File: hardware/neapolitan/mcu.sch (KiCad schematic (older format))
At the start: 60 parts, among them J1 USB-MICRO-B, J11 BARREL_JACK, P1 !IO_INT, P2 !IO_RESET, P20 GPIO, P22 I2S, P28 SD, P5 LEDS, P80 SHIELD, Q5 MOSFET_P, U15 TCA6424A, X2 FOX924B, X3 KT2520, X4 OH4

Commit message: Neapolitan: schematic annotation and cleanup
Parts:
- gave numbers to parts that had none: 16
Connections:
- net ADC0_0: no longer names the net of P20.20 (P20)
- net ADC0_2: no longer names the net of P20.16 (P16)
- net ADC0_6: no longer names the net of P20.14 (P14)
- net CLKOUT: no longer names the net of P22.1 (P1)
- net GCK1: no longer names the net of P28.14 (P14)
- net GCK2: no longer names the net of P28.13 (P13)
- net GPIO3_10: no longer names the net of P20.7 (P7)
- net GPIO3_11: no longer names the net of P20.8 (P8)
- net GPIO3_12: no longer names the net of P20.9 (P9)
- net GPIO3_13: no longer names the net of P20.10 (P10)
- net GPIO3_14: no longer names the net of P20.11 (P11)
- net GPIO3_15: no longer names the net of P20.12 (P12)
- net GPIO3_8: no longer names the net of P20.5 (P5)
- net GPIO3_9: no longer names the net of P20.6 (P6)
- net I2S0_RX_MCLK: no longer names the net of P22.14 (P14)
- net I2S0_RX_SCK: no longer names the net of P22.12 (P12)
- net I2S0_RX_SDA: no longer names the net of P22.13 (P13)
- net I2S0_RX_WS: no longer names the net of P22.15 (P15)
- net I2S0_TX_MCLK: no longer names the net of P22.17 (P17)
- net I2S0_TX_SCK: no longer names the net of P22.16 (P16)
- net P2_13: no longer names the net of P22.22 (P22)
- net P2_8: no longer names the net of P22.23 (P23)
- net P2_9: no longer names the net of P22.21 (P21)
- net RESET: no longer names the net of P22.3 (P3)
- net RTC_ALARM: no longer names the net of P20.2 (P2)
- net SD_CD: no longer names the net of P28.3 (P3)
- net SD_CLK: no longer names the net of P28.11 (P11)
- net U0_RXD: no longer names the net of P22.19 (P19)
- net U0_TXD: no longer names the net of P22.20 (P20)
- net VBAT: no longer names the net of P20.1 (P1)
- net WAKEUP: no longer names the net of P20.4 (P4)
- no-connect marks 17 -> 48
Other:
- note removed: "/I2S0_TX_WS"
- note removed: "I2S0_TX_SDA/"
- moved on the sheet: C68, C69, C71, C72, C73, C74, C75, C76, L10, P1, P2, P20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

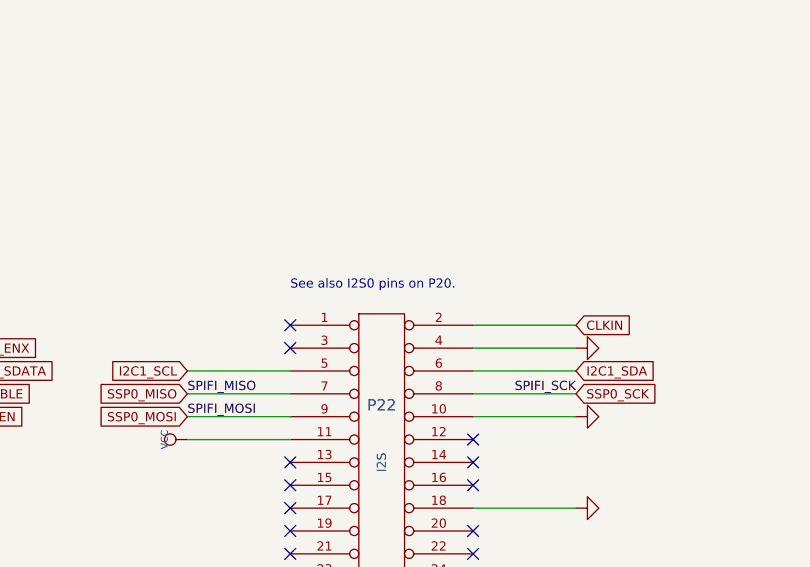
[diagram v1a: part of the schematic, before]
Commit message: Neapolitan: module assignment
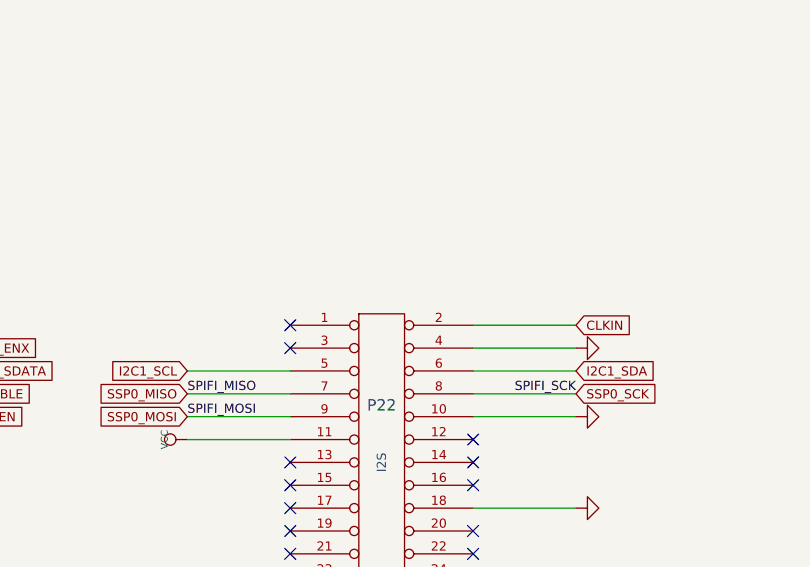
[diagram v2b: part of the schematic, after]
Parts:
- U16: footprint (none) -> gsg-modules:SOT25
- U18: footprint (none) -> gsg-modules:SOT353-1
- X2: footprint (none) -> gsg-modules:XTAL5.0x3.2mm; Description (none) -> OSC TCXO 10.000MHZ HCMOS SMD; Manufacturer (none) -> Fox Electronics; Part Number (none) -> FOX924B-10.000
- X3: footprint (none) -> gsg-modules:KT2520K
- X4: footprint (none) -> gsg-modules:OH4
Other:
- note removed: "See also I2S0 pins on P20."
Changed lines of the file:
@@
 	1    0    0    -1
 $EndComp
-Text Notes 9300 8100 0    40   ~ 0
-See also I2S0 pins on P20.
 Text GLabel 5500 3500 0    40   Input ~ 0
 MIX_BYPASS
@@
 F 0 "X2" H 9050 5050 60  0000 C CNN
 F 1 "FOX924B" H 9050 4750 60  0000 C CNN
-F 2 "" H 9050 4900 60  0000 C CNN
+F 2 "gsg-modules:XTAL5.0x3.2mm" H 9050 4900 60  0001 C CNN
 F 3 "" H 9050 4900 60  0000 C CNN
+F 4 "Fox Electronics" H 9050 4900 60  0001 C CNN "Manufacturer"
+F 5 "FOX924B-10.000" H 9050 4900 60  0001 C CNN "Part Number"
+F 6 "OSC TCXO 10.000MHZ HCMOS SMD" H 9050 4900 60  0001 C CNN "Description"
 	1    9050 4900
 	1    0    0    -1
@@
 F 0 "X3" H 11200 5800 60  0000 C CNN
 F 1 "KT2520" H 11200 5400 60  0000 C CNN
-F 2 "" H 11200 5600 60  0000 C CNN
+F 2 "gsg-modules:KT2520K" H 11200 5600 60  0001 C CNN
 F 3 "" H 11200 5600 60  0000 C CNN
 F 4 "AVX" H 11200 5600 60  0001 C CNN "Manufacturer"
@@
 F 0 "U16" H 11200 5100 40  0000 C CNN
 F 1 "TCR2EF" H 11200 4700 40  0000 C CNN
-F 2 "" H 11200 4900 40  0000 C CNN
+F 2 "gsg-modules:SOT25" H 11200 4900 40  0001 C CNN
 F 3 "" H 11200 4900 40  0000 C CNN
 F 4 "Toshiba" H 11200 4900 60  0001 C CNN "Manufacturer"
@@
 F 0 "U18" H 12895 5815 40  0000 C CNN
 F 1 "74LVC1G14" H 12950 5600 40  0000 C CNN
-F 2 "" H 12845 5565 30  0000 C CNN
+F 2 "gsg-modules:SOT353-1" H 12845 5565 30  0001 C CNN
 F 3 "" H 12895 5815 60  0000 C CNN
 F 4 "NXP" H 12750 5700 60  0001 C CNN "Manufacturer"
@@
 F 0 "X4" H 14700 4950 60  0000 C CNN
 F 1 "OH4" H 14700 4650 60  0000 C CNN
-F 2 "" H 14700 4800 60  0000 C CNN
+F 2 "gsg-modules:OH4" H 14700 4800 60  0001 C CNN
 F 3 "" H 14700 4800 60  0000 C CNN
 F 4 "Connor-Winfield" H 14700 4800 60  0001 C CNN "Manufacturer"

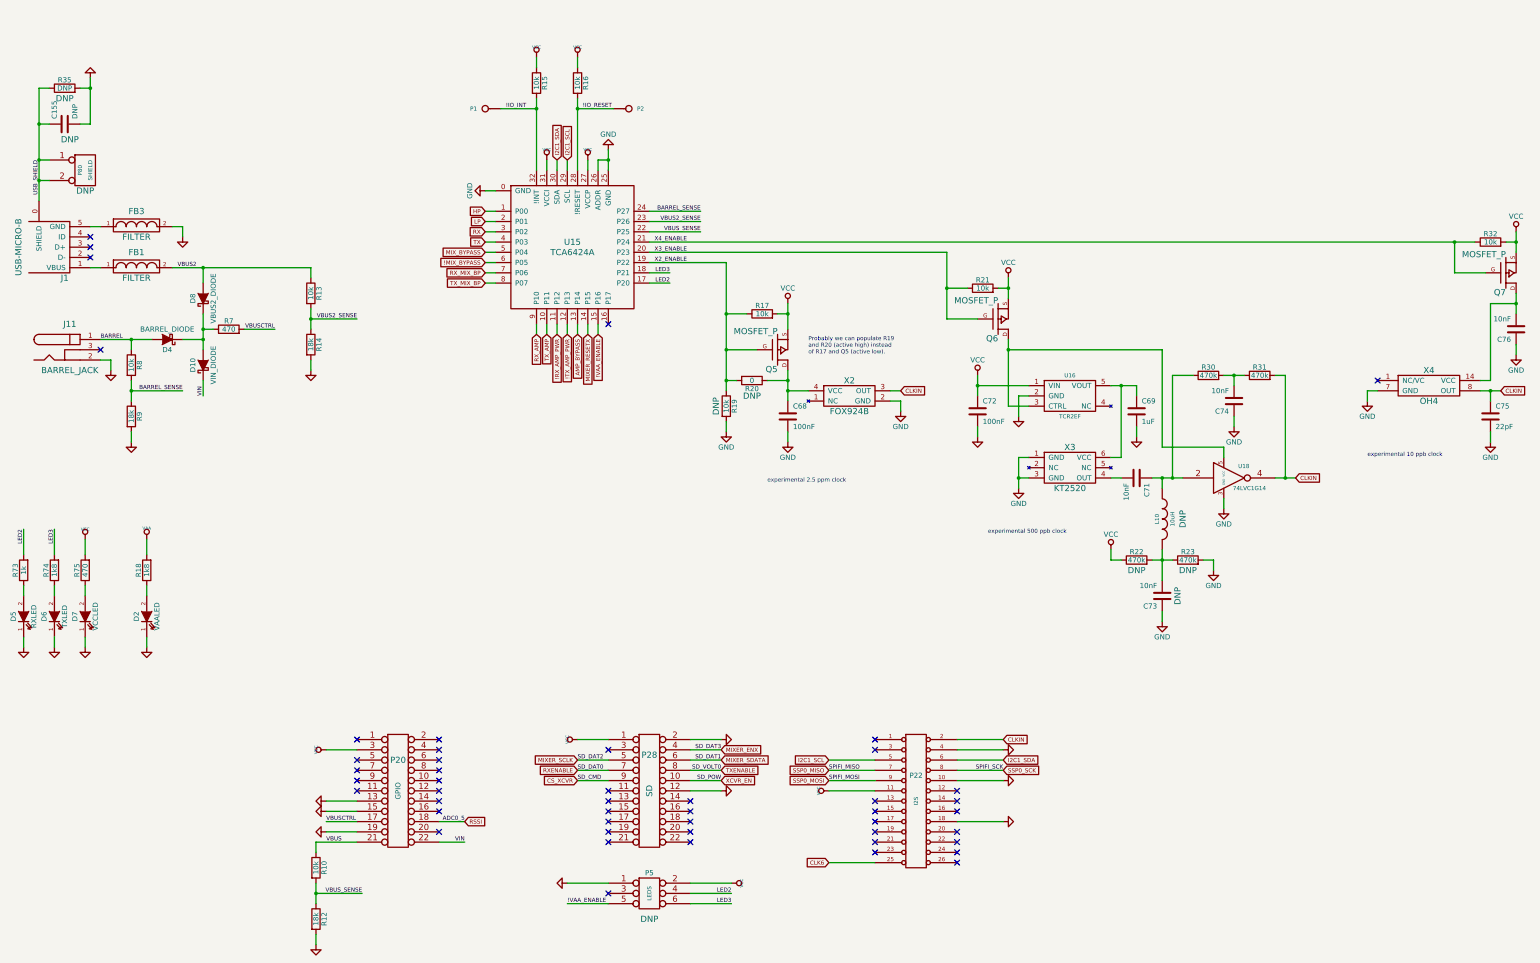
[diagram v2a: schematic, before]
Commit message: Neapolitan: completed initial layout
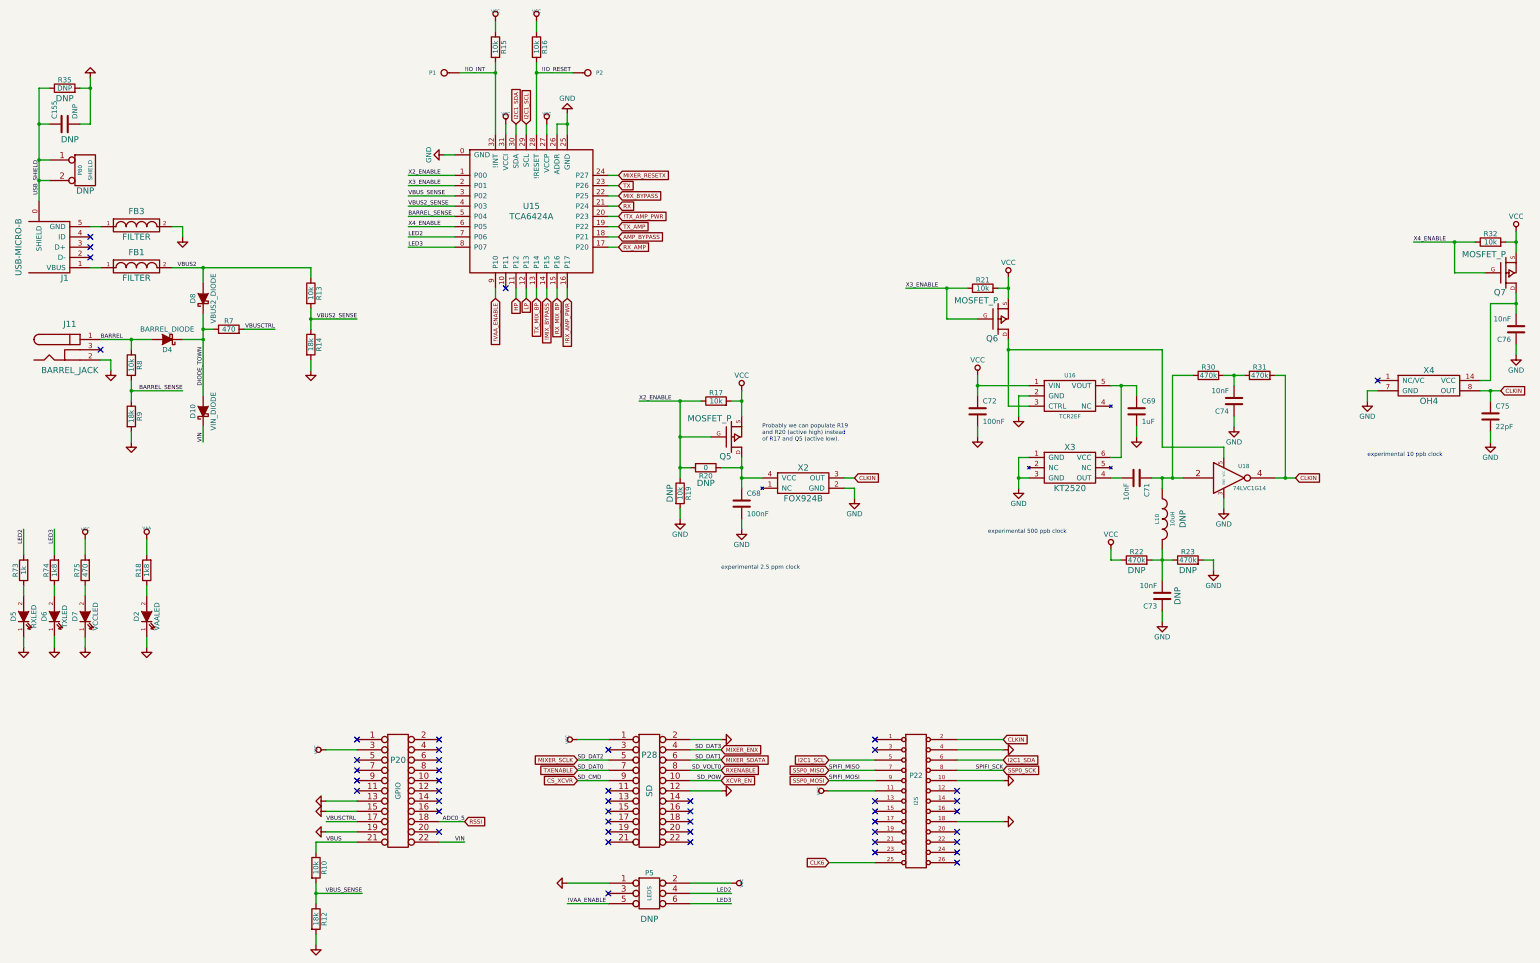
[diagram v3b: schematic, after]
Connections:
- net !MIX_BYPASS: now also U15.14 (P15); no longer U15.6 (P05)
- net !RX_AMP_PWR: now also U15.16 (P17); no longer U15.11 (P12)
- net !TX_AMP_PWR: now also U15.20 (P23); no longer U15.12 (P13)
- net !VAA_ENABLE: now also U15.9 (P10); no longer U15.15 (P16)
- net AMP_BYPASS: now also U15.18 (P21); no longer U15.13 (P14)
- net BARREL_SENSE: now also U15.5 (P04); no longer U15.24 (P27)
- net HP: now also U15.11 (P12); no longer U15.1 (P00)
- net LED2: now also U15.7 (P06); no longer U15.17 (P20)
- net LED3: now also U15.8 (P07); no longer U15.18 (P21)
- net LP: now also U15.12 (P13); no longer U15.2 (P01)
- net MIXER_RESETX: now also U15.24 (P27); no longer U15.14 (P15)
- net MIX_BYPASS: now also U15.22 (P25); no longer U15.5 (P04)
- net RX: now also U15.21 (P24); no longer U15.3 (P02)
- net RXENABLE: now also P28.8 (P8); no longer P28.7 (P7)
- net RX_AMP: now also U15.17 (P20); no longer U15.9 (P10)
- net RX_MIX_BP: now also U15.15 (P16); no longer U15.7 (P06)
- net TX: now also U15.23 (P26); no longer U15.4 (P03)
- net TXENABLE: now also P28.7 (P7); no longer P28.8 (P8)
- net TX_AMP: now also U15.19 (P22); no longer U15.10 (P11)
- net TX_MIX_BP: now also U15.13 (P14); no longer U15.8 (P07)
- net VBUS2_SENSE: now also U15.4 (P03); no longer U15.23 (P26)
- net VBUS_SENSE: now also U15.3 (P02); no longer U15.22 (P25)
- net X2_ENABLE: now also U15.1 (P00); no longer U15.19 (P22)
- net X3_ENABLE: now also U15.2 (P01); no longer U15.20 (P23)
- net X4_ENABLE: now also U15.6 (P05); no longer U15.21 (P24)
- net DIODE_TOWN: now reaches D10.2 (A), D4.1 (K), D8.1 (K), R7.1
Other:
- moved on the sheet: C68, D10, P1, P2, Q5, R15, R16, R17, R19, R20, U15, X2

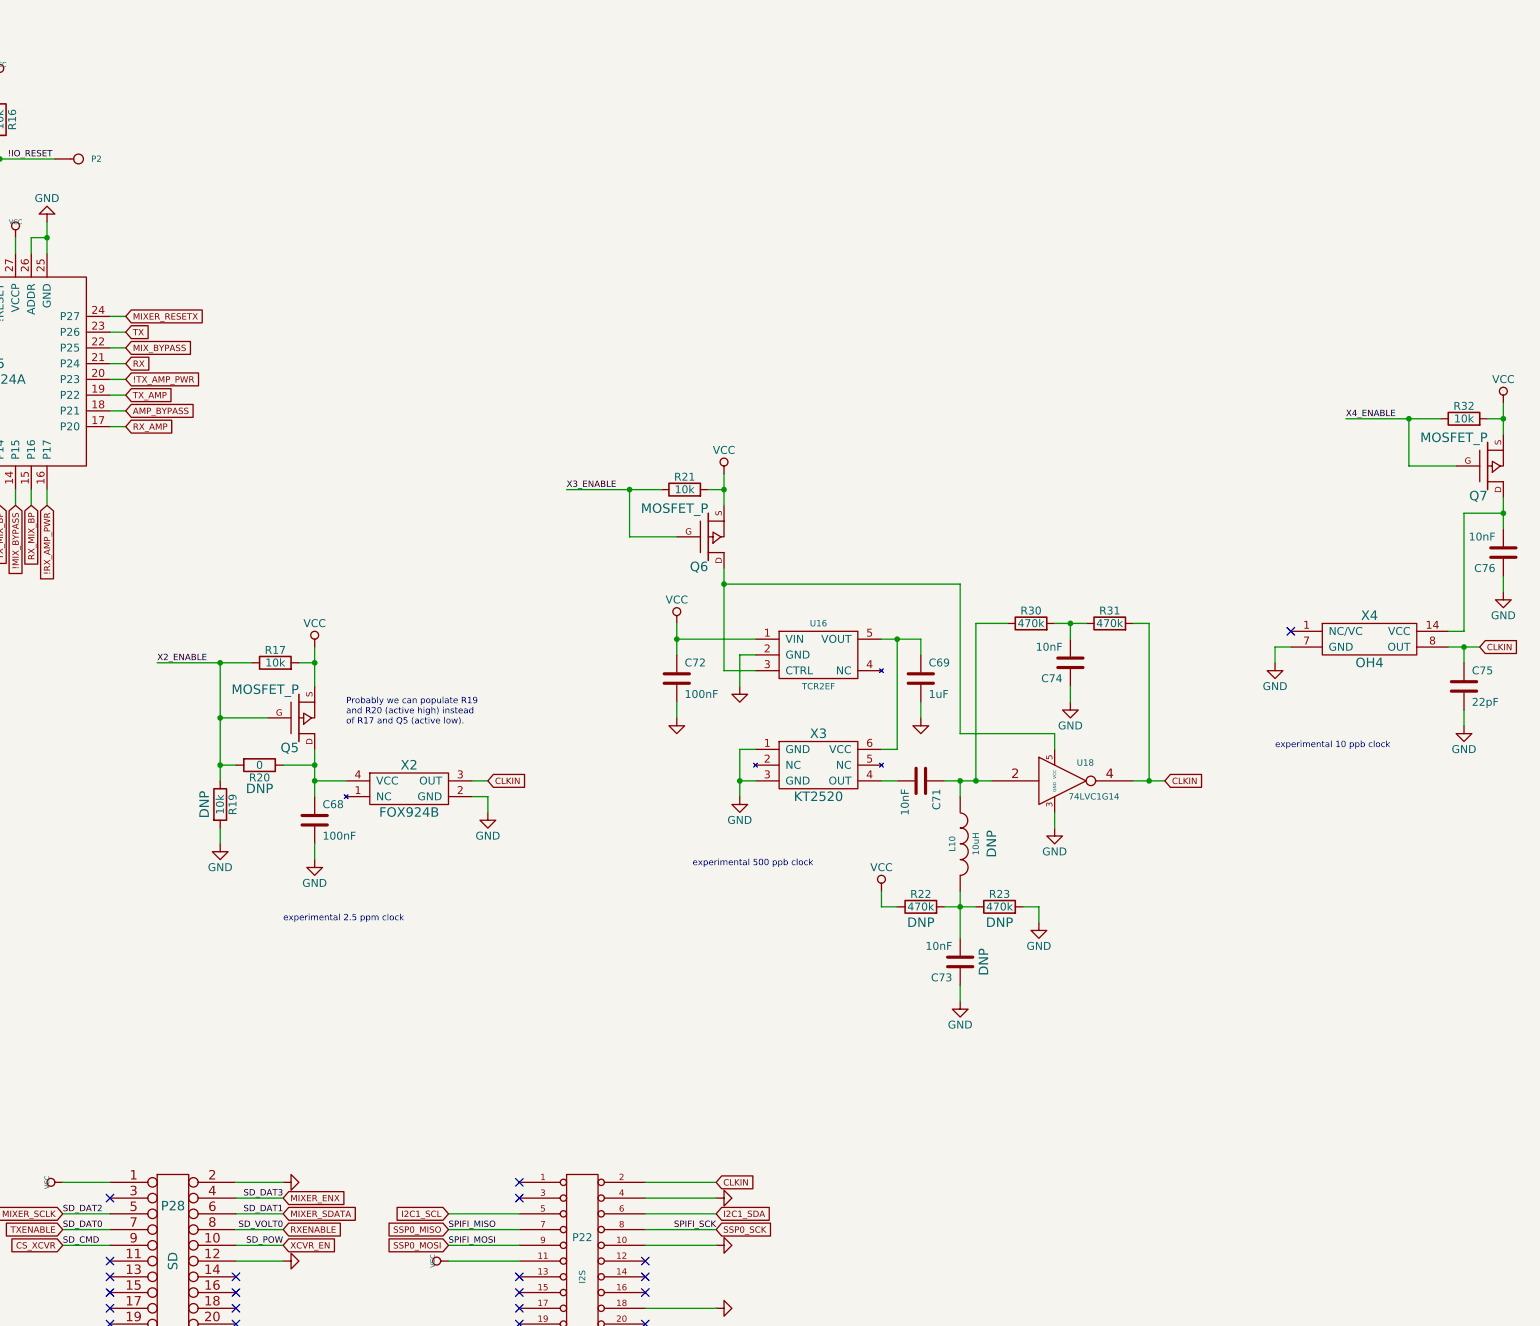
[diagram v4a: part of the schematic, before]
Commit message: Neapolitan: added decoupling caps for U15 and U18
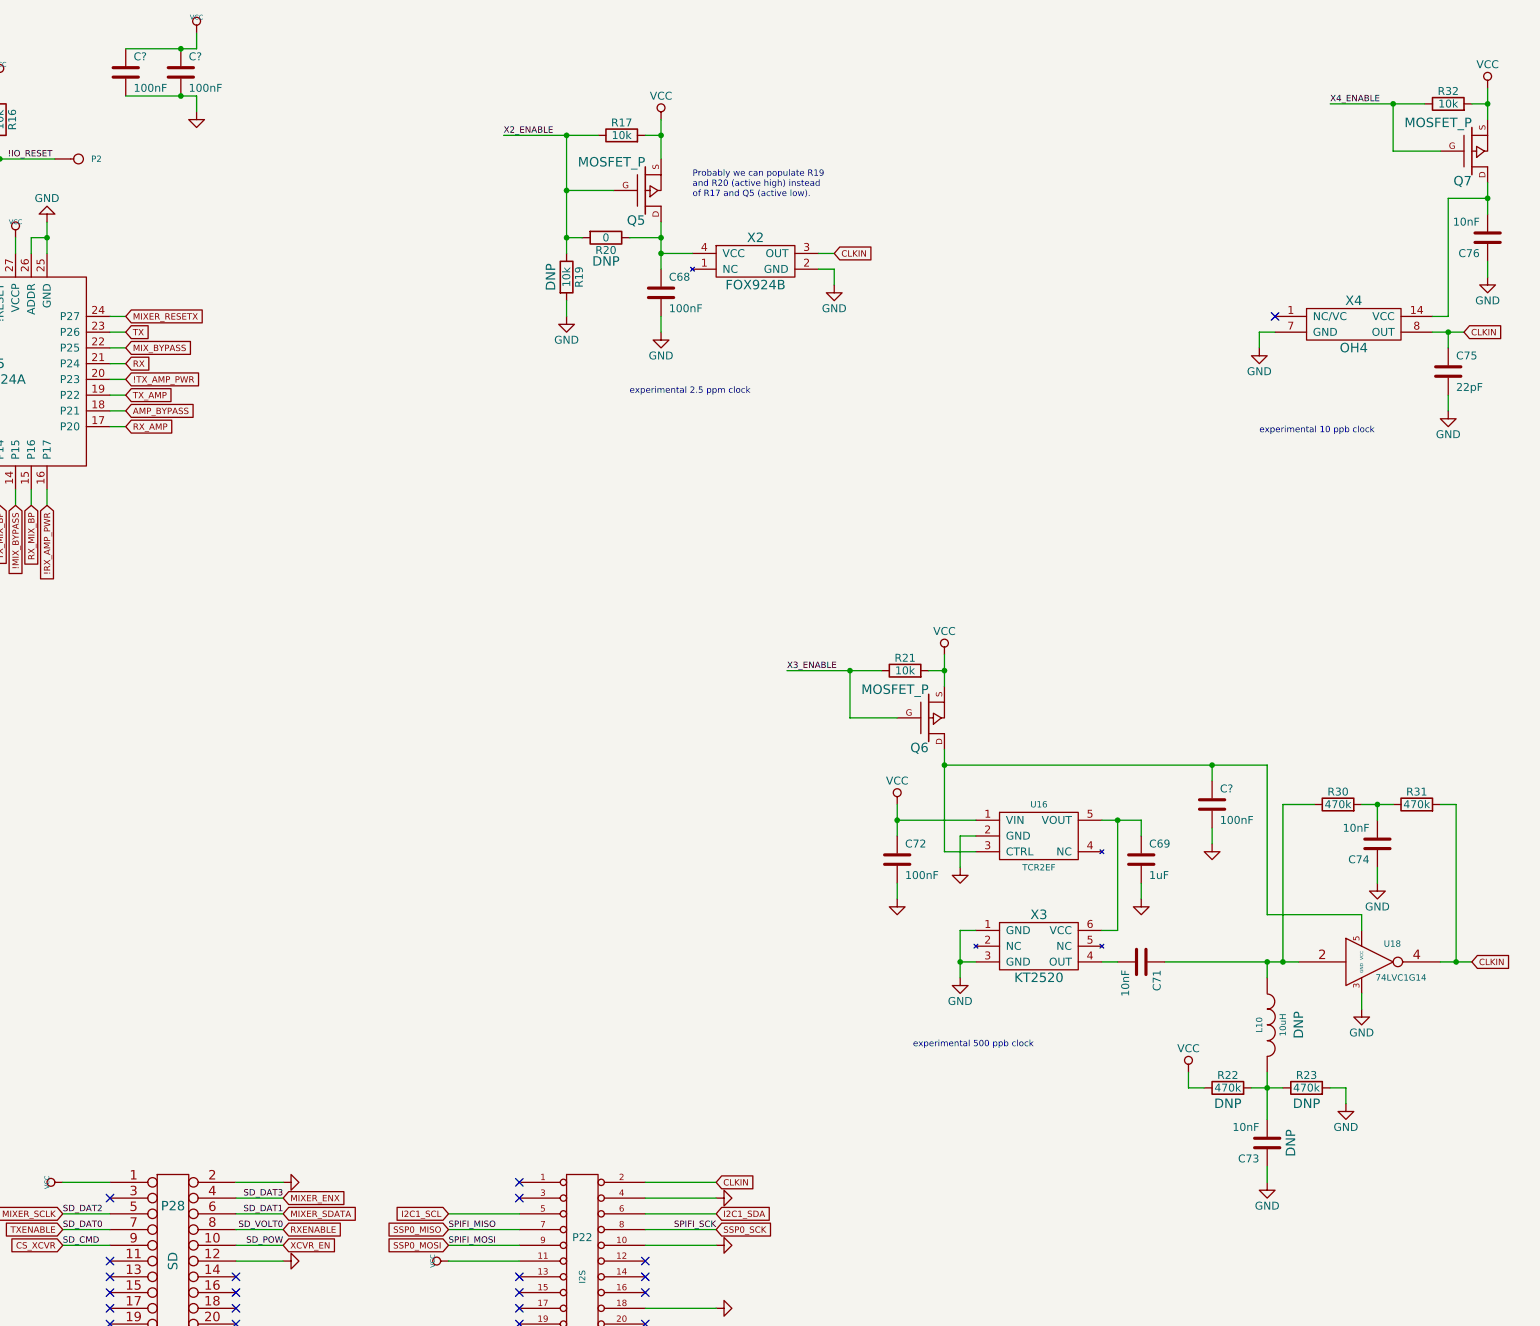
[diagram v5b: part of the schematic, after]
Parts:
- added C? (x3): 100nF, hackrf:GSG-0402, symbol C
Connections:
- net GND: now also C?.2, C?.2, C?.2
- net VCC: now also C?.1, C?.1
- net at Q6.D, U16.3 (CTRL), U18.5 (VCC): now also C?.1
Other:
- moved on the sheet: C68, C69, C71, C72, C73, C74, C75, C76, L10, Q5, Q6, Q7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
